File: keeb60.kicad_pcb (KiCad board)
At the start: 2 copper layers, 123 parts, among them K000 Esc, K001 1, K002 2, K003 3, K004 4, K005 5, K006 6, K007 7, K008 8, K009 9, K010 0, K011 _, K012 =, K013 Backspace, K100 Tab, K101 Q, K102 W, K103 E, K104 R, K105 T, K106 Y, K107 U, K108 I, K109 O, K110 P, K111 [, K112 ], K113 Pipe, K200 Caps Lock, K201 A, K202 S, K203 D, K204 F, K205 G, K206 H, K207 J, K208 K, K209 L, K210 ;, K211 ,, K213 Enter, K300 Shift, K302 Z, K303 X, K304 C, K305 V, K306 B, K307 N, K308 M, K309 ,, K310 ., K311 /, K313 Shift, K400 Ctrl, K401 Option, K402 Command, K406 Space, K410 Command, K411 Option, K412 Function, K413 Ctrl, U1 ProMicro

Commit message: Add edge cut
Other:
- board outline added: 290 x 99.3 mm
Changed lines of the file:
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@@
 		)
+	)
+	(gr_rect
+		(start 49.46875 84.51875)
+		(end 339.46875 183.76875)
+		(stroke
+			(width 0.05)
+			(type solid)
+		)
+		(fill no)
+		(layer "Edge.Cuts")
 	)
 	(embedded_fonts no)

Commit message: thangs
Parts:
- moved D52 73.8 mm to (242.9, 158.0)
- moved D49 38.1 mm to (281.0, 158.0)
- moved D51 35.7 mm to (316.7, 158.0)
- turned D16 to 90 degrees
- turned D43 to 90 degrees
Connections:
- D0 pad 1: (no net) -> Row0
- D0 pad 2: (no net) -> Net-(D0-A)
- D1 pad 1: (no net) -> Row0
- D1 pad 2: (no net) -> Net-(D1-A)
- D10 pad 1: (no net) -> Row0
- D10 pad 2: (no net) -> Net-(D10-A)
- D11 pad 1: (no net) -> Row0
- D11 pad 2: (no net) -> Net-(D11-A)
- D12 pad 1: (no net) -> Row0
- D12 pad 2: (no net) -> Net-(D12-A)
- D13 pad 1: (no net) -> Row1
- D13 pad 2: (no net) -> Net-(D13-A)
- D14 pad 1: (no net) -> Row1
- D14 pad 2: (no net) -> Net-(D14-A)
- D15 pad 1: (no net) -> Row1
- D15 pad 2: (no net) -> Net-(D15-A)
- D16 pad 1: (no net) -> Row1
- D16 pad 2: (no net) -> Net-(D16-A)
- D17 pad 1: (no net) -> Row1
- D17 pad 2: (no net) -> Net-(D17-A)
- D18 pad 1: (no net) -> Row1
- D18 pad 2: (no net) -> Net-(D18-A)
- D19 pad 1: (no net) -> Row1
- D19 pad 2: (no net) -> Net-(D19-A)
- D2 pad 1: (no net) -> Row0
- D2 pad 2: (no net) -> Net-(D2-A)
- D20 pad 1: (no net) -> Row1
- D20 pad 2: (no net) -> Net-(D20-A)
- D21 pad 1: (no net) -> Row1
- D21 pad 2: (no net) -> Net-(D21-A)
- D22 pad 1: (no net) -> Row1
- D22 pad 2: (no net) -> Net-(D22-A)
- D23 pad 1: (no net) -> Row1
- D23 pad 2: (no net) -> Net-(D23-A)
- D24 pad 1: (no net) -> Row1
- D24 pad 2: (no net) -> Net-(D24-A)
- D25 pad 1: (no net) -> Row1
- D25 pad 2: (no net) -> Net-(D25-A)
- D26 pad 1: (no net) -> Row2
- D26 pad 2: (no net) -> Net-(D26-A)
- D27 pad 1: (no net) -> Row2
- D27 pad 2: (no net) -> Net-(D27-A)
- D28 pad 1: (no net) -> Row2
- D28 pad 2: (no net) -> Net-(D28-A)
- D29 pad 1: (no net) -> Row2
- D29 pad 2: (no net) -> Net-(D29-A)
- D3 pad 1: (no net) -> Row0
- D3 pad 2: (no net) -> Net-(D3-A)
- D30 pad 1: (no net) -> Row2
- D30 pad 2: (no net) -> Net-(D30-A)
- D31 pad 1: (no net) -> Row2
- D31 pad 2: (no net) -> Net-(D31-A)
- D32 pad 1: (no net) -> Row2
- D32 pad 2: (no net) -> Net-(D32-A)
- D33 pad 1: (no net) -> Row2
- D33 pad 2: (no net) -> Net-(D33-A)
- D34 pad 1: (no net) -> Row2
- D34 pad 2: (no net) -> Net-(D34-A)
- D35 pad 1: (no net) -> Row2
- D35 pad 2: (no net) -> Net-(D35-A)
- D36 pad 1: (no net) -> Row2
- D36 pad 2: (no net) -> Net-(D36-A)
- D37 pad 1: (no net) -> Row2
- D37 pad 2: (no net) -> Net-(D37-A)
- D38 pad 1: (no net) -> Row2
- D38 pad 2: (no net) -> Net-(D38-A)
- D39 pad 1: (no net) -> Row3
- D39 pad 2: (no net) -> Net-(D39-A)
- D4 pad 1: (no net) -> Row0
- D4 pad 2: (no net) -> Net-(D4-A)
- D40 pad 1: (no net) -> Row3
- D40 pad 2: (no net) -> Net-(D40-A)
- D41 pad 1: (no net) -> Row3
- D41 pad 2: (no net) -> Net-(D41-A)
- D42 pad 1: (no net) -> Row3
- D42 pad 2: (no net) -> Net-(D42-A)
- D43 pad 1: (no net) -> Row3
- D43 pad 2: (no net) -> Net-(D43-A)
- D44 pad 1: (no net) -> Row3
- D44 pad 2: (no net) -> Net-(D44-A)
- D45 pad 1: (no net) -> Row3
- D45 pad 2: (no net) -> Net-(D45-A)
- D46 pad 1: (no net) -> Row3
- D46 pad 2: (no net) -> Net-(D46-A)
- D47 pad 1: (no net) -> Row3
- D47 pad 2: (no net) -> Net-(D47-A)
- D48 pad 1: (no net) -> Row3
- D48 pad 2: (no net) -> Net-(D48-A)
- D49 pad 1: (no net) -> Row3
- D49 pad 2: (no net) -> Net-(D49-A)
- D5 pad 1: (no net) -> Row0
- D5 pad 2: (no net) -> Net-(D5-A)
- D50 pad 1: (no net) -> Row3
- D50 pad 2: (no net) -> Net-(D50-A)
- D53 pad 1: (no net) -> Row4
- D53 pad 2: (no net) -> Net-(D53-A)
- D54 pad 1: (no net) -> Row4
- D54 pad 2: (no net) -> Net-(D54-A)
- D55 pad 1: (no net) -> Row4
- D55 pad 2: (no net) -> Net-(D55-A)
- D56 pad 1: (no net) -> Row4
- D56 pad 2: (no net) -> Net-(D56-A)
- D57 pad 1: (no net) -> Row4
- D57 pad 2: (no net) -> Net-(D57-A)
- D58 pad 1: (no net) -> Row4
- D58 pad 2: (no net) -> Net-(D58-A)
- D59 pad 1: (no net) -> Row4
- D59 pad 2: (no net) -> Net-(D59-A)
- D6 pad 1: (no net) -> Row0
- D6 pad 2: (no net) -> Net-(D6-A)
- D60 pad 1: (no net) -> Row4
- D60 pad 2: (no net) -> Net-(D60-A)
- D7 pad 1: (no net) -> Row0
- D7 pad 2: (no net) -> Net-(D7-A)
- D8 pad 1: (no net) -> Row0
- D8 pad 2: (no net) -> Net-(D8-A)
- D9 pad 1: (no net) -> Row0
- D9 pad 2: (no net) -> Net-(D9-A)
- K101 pad 1: (no net) -> Net-(D14-A)
- K101 pad 2: (no net) -> Col1
- K204 pad 1: (no net) -> Net-(D30-A)
- K204 pad 2: (no net) -> Col4
- K209 pad 1: (no net) -> Net-(D35-A)
- K209 pad 2: (no net) -> Col9
- U1 pad 24: Net-(U1-5V) -> unconnected-(U1-5V-Pad24)
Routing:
- net Row0: track 0.00 -> 228.6 mm
- net Row1: track 0.00 -> 214.3 mm
- net Row3: track 0.00 -> 203.1 mm
- net Row2: track 0.00 -> 197.6 mm
- net Col0: track 0.00 -> 89.2 mm
- net Col10: track 0.00 -> 48.2 mm
- net Col9: track 0.00 -> 48.1 mm
- net Col4: track 0.00 -> 48.1 mm
- net Col3: track 0.00 -> 48.1 mm
- net Col6: track 0.00 -> 48.1 mm
- net Col2: track 0.00 -> 48.1 mm
- net Col11: track 0.00 -> 48.1 mm
- net Col5: track 0.00 -> 48.1 mm
- net Col8: track 0.00 -> 48.1 mm
- net Col7: track 0.00 -> 48.1 mm
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
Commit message: Fix diodes
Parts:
- moved D13 253.1 mm to (71.4, 119.9)
- moved D51 247.6 mm to (69.8, 177.0)
- moved D26 231.8 mm to (73.8, 138.9)
- moved D27 229.4 mm to (100.0, 138.9)
- moved D40 212.8 mm to (109.5, 158.0)
- moved D39 212.8 mm to (78.6, 158.0)
- moved D52 151.2 mm to (92.9, 177.0)
- moved D55 142.9 mm to (259.6, 177.0)
- moved D54 95.2 mm to (188.1, 177.0)
- moved D56 95.2 mm to (283.4, 177.0)
- moved D60 76.5 mm to (323.9, 100.9)
- moved D59 61.0 mm to (328.6, 119.9)
- moved D50 54.8 mm to (316.7, 158.0)
- moved D41 50.8 mm to (129.4, 158.0)
- moved D38 50.0 mm to (321.5, 138.9)
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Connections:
- D13 pad 1: Row1 -> (no net)
- D13 pad 2: Net-(D13-A) -> (no net)
- D26 pad 1: Row2 -> (no net)
- D26 pad 2: Net-(D26-A) -> (no net)
- D28 pad 1: Row2 -> (no net)
- D28 pad 2: Net-(D28-A) -> (no net)
- D30 pad 1: Row2 -> (no net)
- D30 pad 2: Net-(D30-A) -> (no net)
- D39 pad 1: Row3 -> (no net)
- D39 pad 2: Net-(D39-A) -> (no net)
- D40 pad 1: Row3 -> (no net)
- D40 pad 2: Net-(D40-A) -> (no net)
- D41 pad 1: Row3 -> (no net)
- D41 pad 2: Net-(D41-A) -> (no net)
- D42 pad 1: Row3 -> (no net)
- D42 pad 2: Net-(D42-A) -> (no net)
- D50 pad 1: Row3 -> (no net)
- D50 pad 2: Net-(D50-A) -> (no net)
- D59 pad 1: Row4 -> (no net)
- D59 pad 2: Net-(D59-A) -> (no net)
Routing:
- net Row1: track 214.3 -> 233.4 mm

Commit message: More routing
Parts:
- moved U1 2.80 mm to (210.8, 173.5), turned to -90 degrees
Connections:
- D13 pad 1: (no net) -> Row1
- D13 pad 2: (no net) -> Net-(D13-A)
- D26 pad 1: (no net) -> Row2
- D26 pad 2: (no net) -> Net-(D26-A)
- D28 pad 1: (no net) -> Row2
- D28 pad 2: (no net) -> Net-(D28-A)
- D30 pad 1: (no net) -> Row2
- D30 pad 2: (no net) -> Net-(D30-A)
- D39 pad 1: (no net) -> Row3
- D39 pad 2: (no net) -> Net-(D39-A)
- D40 pad 1: (no net) -> Row3
- D40 pad 2: (no net) -> Net-(D40-A)
- D41 pad 1: (no net) -> Row3
- D41 pad 2: (no net) -> Net-(D41-A)
- D42 pad 1: (no net) -> Row3
- D42 pad 2: (no net) -> Net-(D42-A)
- D50 pad 1: (no net) -> Row3
- D50 pad 2: (no net) -> Net-(D50-A)
- D51 pad 1: (no net) -> Row4
- D51 pad 2: (no net) -> Net-(D51-A)
- D52 pad 1: (no net) -> Row4
- D52 pad 2: (no net) -> Net-(D52-A)
- D59 pad 1: (no net) -> Row4
- D59 pad 2: (no net) -> Net-(D59-A)
- K302 pad 2: Col2 -> Col1
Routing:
- net Row4: track 0.00 -> 71.4 mm
- net Col1: track 48.1 -> 100.4 mm
- net Col6: track 48.1 -> 92.9 mm
- net Col9: track 48.1 -> 71.1 mm
- net Col8: track 48.1 -> 71.1 mm
- net Col7: track 48.1 -> 71.1 mm
- net Col4: track 48.1 -> 71.1 mm
- net Col11: track 48.1 -> 71.1 mm
- net Col3: track 48.1 -> 71.1 mm
- net Col5: track 48.1 -> 71.1 mm
- net Col10: track 48.2 -> 71.2 mm
- net Row2: track 197.6 -> 216.7 mm
- net Row3: track 203.1 -> 203.8 mm

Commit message: ROUTING!
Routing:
- net Row4: track 71.4 -> 191.1 mm
- net Row3: track 203.8 -> 240.9 mm
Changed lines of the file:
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@@
+	)
+	(segment
+		(start 288.8625 159.60625)
+		(end 280.9875 159.60625)
+		(width 0.254)
+		(layer "B.Cu")
+		(net 45)
+	)
+	(segment
+		(start 315.05625 157.95625)
+		(end 290.5125 157.95625)
+		(width 0.254)
+		(layer "B.Cu")
+		(net 45)
+	)
+	(segment
+		(start 290.5125 157.95625)
+		(end 288.8625 159.60625)
+		(width 0.254)
+		(layer "B.Cu")
+		(net 45)
 	)
 	(segment
@@
 	)
 	(segment
+		(start 316.70625 159.60625)
+		(end 315.05625 157.95625)
+		(width 0.254)
+		(layer "B.Cu")
+		(net 45)
+	)
+	(segment
 		(start 59.53125 140.462)
 		(end 67.183 148.11375)
@@
 	)
 	(segment
+		(start 122.175 178.65625)
+		(end 116.68125 178.65625)
+		(width 0.254)
+		(layer "B.Cu")
+		(net 82)
+	)
+	(segment
+		(start 180.975 177.00625)
+		(end 123.825 177.00625)
+		(width 0.254)
+		(layer "B.Cu")
+		(net 82)
+	)
+	(segment
+		(start 69.85 178.65625)
+		(end 116.68125 178.65625)
+		(width 0.254)
+		(layer "B.Cu")
+		(net 82)
+	)
+	(segment
+		(start 188.11875 178.65625)
+		(end 182.625 178.65625)
+		(width 0.254)
+		(layer "B.Cu")
+		(net 82)
+	)
+	(segment
 		(start 330.99375 178.65625)
 		(end 259.55625 178.65625)
 		(width 0.254)
 		(layer "B.Cu")
+		(net 82)
+	)
+	(segment
+		(start 182.625 178.65625)
+		(end 180.975 177.00625)
+		(width 0.254)
+		(layer "B.Cu")
+		(net 82)
+	)
+	(segment
+		(start 123.825 177.00625)
+		(end 122.175 178.65625)
+		(width 0.254)
+		(layer "B.Cu")

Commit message: ROUTES BBY
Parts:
- moved U1 2.97 mm to (210.0, 170.7), turned to 90 degrees
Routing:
- net Row4: track 191.1 -> 279.3 mm
- net Col12: track 24.7 -> 79.3 mm
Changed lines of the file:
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@@
 	(footprint "TheOneProMicro-main:TheOneProMicro"
 		(layer "F.Cu")
-		(at 210.82 173.51375 -90)
+		(at 210.02625 170.65625 90)
 		(descr "Pro Micro footprint")
 		(tags "promicro ProMicro")
@@
 		)
 		(property "Datasheet" ""
-			(at -1.27 1.27 180)
+			(at -1.27 1.27 0)
 			(unlocked yes)
 			(layer "F.Fab")
@@
 		)
 		(property "Description" ""
-			(at -1.27 1.27 180)
+			(at -1.27 1.27 0)
 			(unlocked yes)
 			(layer "F.Fab")
@@
 		)
 		(pad "1" thru_hole circle
-			(at 6.35 -12.7 180)
+			(at 6.35 -12.7)
 			(size 1.6 1.6)
 			(drill 1.1)
@@
 		)
 		(pad "2" thru_hole circle
-			(at 6.35 -10.16 180)
+			(at 6.35 -10.16)
 			(size 1.6 1.6)
 			(drill 1.1)
@@
 		)
 		(pad "3" thru_hole circle
-			(at 6.35 -7.62 180)
+			(at 6.35 -7.62)
 			(size 1.6 1.6)
 			(drill 1.1)
@@
 		)
 		(pad "4" thru_hole circle
-			(at 6.35 -5.08 180)
+			(at 6.35 -5.08)
 			(size 1.6 1.6)
 			(drill 1.1)
@@
 		)
 		(pad "5" thru_hole circle
-			(at 6.35 -2.54 180)
+			(at 6.35 -2.54)
 			(size 1.6 1.6)
 			(drill 1.1)
@@
 		)
 		(pad "6" thru_hole circle
-			(at 6.35 0 180)
+			(at 6.35 0)
 			(size 1.6 1.6)
 			(drill 1.1)
@@
 		)
 		(pad "7" thru_hole circle
-			(at 6.35 2.54 180)
+			(at 6.35 2.54)
 			(size 1.6 1.6)
 			(drill 1.1)
@@
 		)
 		(pad "8" thru_hole circle
-			(at 6.35 5.08 180)
+			(at 6.35 5.08)
 			(size 1.6 1.6)
 			(drill 1.1)
@@
 		)
 		(pad "9" thru_hole circle
-			(at 6.35 7.62 180)
+			(at 6.35 7.62)
 			(size 1.6 1.6)
 			(drill 1.1)
@@
 		)
 		(pad "10" thru_hole circle
-			(at 6.35 10.16 180)
+			(at 6.35 10.16)
 			(size 1.6 1.6)
 			(drill 1.1)
@@
 		)
 		(pad "11" thru_hole circle
-			(at 6.35 12.7 180)
+			(at 6.35 12.7)
 			(size 1.6 1.6)
 			(drill 1.1)
@@
 		)
 		(pad "12" thru_hole circle
-			(at 6.35 15.24 180)
+			(at 6.35 15.24)
 			(size 1.6 1.6)
 			(drill 1.1)
@@
 		)
 		(pad "13" thru_hole circle
-			(at -8.89 15.24 180)
+			(at -8.89 15.24)
 			(size 1.6 1.6)
 			(drill 1.1)
@@
 		)
 		(pad "14" thru_hole circle
-			(at -8.89 12.7 180)
+			(at -8.89 12.7)
 			(size 1.6 1.6)
 			(drill 1.1)
@@
 		)
 		(pad "15" thru_hole circle
-			(at -8.89 10.16 180)
+			(at -8.89 10.16)
 			(size 1.6 1.6)
 			(drill 1.1)
@@
 		)
 		(pad "16" thru_hole circle
-			(at -8.89 7.62 180)
+			(at -8.89 7.62)
 			(size 1.6 1.6)
 			(drill 1.1)
@@
 		)
 		(pad "17" thru_hole circle
-			(at -8.89 5.08 180)
+			(at -8.89 5.08)
 			(size 1.6 1.6)
 			(drill 1.1)
@@
 		)
 		(pad "18" thru_hole circle
-			(at -8.89 2.54 180)
+			(at -8.89 2.54)
 			(size 1.6 1.6)
 			(drill 1.1)
@@
 		)
 		(pad "19" thru_hole circle
-			(at -8.89 0 180)
+			(at -8.89 0)
 			(size 1.6 1.6)
 			(drill 1.1)
@@
 		)
 		(pad "20" thru_hole circle
-			(at -8.89 -2.54 180)
+			(at -8.89 -2.54)
 			(size 1.6 1.6)
 			(drill 1.1)
@@
 		)
 		(pad "21" thru_hole circle
-			(at -8.89 -5.08 180)
+			(at -8.89 -5.08)
 			(size 1.6 1.6)
 			(drill 1.1)
@@
 		)
 		(pad "22" thru_hole circle
-			(at -8.89 -7.62 180)
+			(at -8.89 -7.62)
 			(size 1.6 1.6)
 			(drill 1.1)
@@
 		)
 		(pad "23" thru_hole circle
-			(at -8.89 -10.16 180)
+			(at -8.89 -10.16)
 			(size 1.6 1.6)
 			(drill 1.1)
@@
 		)
 		(pad "24" thru_hole rect
-			(at -8.89 -12.7 180)
+			(at -8.89 -12.7)
 			(size 1.6 1.6)
 			(drill 1.1)
@@
 	)
 	(segment
+		(start 302.41875 130.96875)
+		(end 308.1655 130.96875)
+		(width 0.254)
+		(layer "F.Cu")
+		(net 78)
+	)
+	(segment
+		(start 310.0705 129.06375)
+		(end 307.975 131.15925)
+		(width 0.254)
+		(layer "F.Cu")
+		(net 78)
+	)
+	(segment
+		(start 292.93085 121.48085)
+		(end 302.41875 130.96875)
+		(width 0.254)
+		(layer "F.Cu")
+		(net 78)
+	)
+	(segment
+		(start 308.1655 130.96875)
+		(end 310.0705 129.06375)
+		(width 0.254)
+		(layer "F.Cu")
+		(net 78)
+	)
+	(segment
+		(start 293.40175 110.01375)
+		(end 292.93085 110.48465)
+		(width 0.254)
+		(layer "F.Cu")
+		(net 78)
+	)
+	(segment
+		(start 292.93085 110.48465)
+		(end 292.93085 121.48085)
+		(width 0.254)
+		(layer "F.Cu")
+		(net 78)
+	)
+	(segment
 		(start 281.78125 98.39325)
 		(end 293.40175 110.01375)
@@
 	)
 	(segment
+		(start 307.975 145.44675)
+		(end 305.308 148.11375)
+		(width 0.254)
+		(layer "F.Cu")
+		(net 78)
+	)
+	(segment
 		(start 281.78125 93.05925)
 		(end 281.78125 98.39325)
@@
 	)
 	(segment
+		(start 307.975 131.15925)
+		(end 307.975 145.44675)
+		(width 0.254)
+		(layer "F.Cu")
+		(net 78)
+	)
+	(segment
+		(start 333.375 116.74375)
+		(end 328.6125 121.50625)
+		(width 0.2)
+		(layer "B.Cu")
+		(net 82)
+	)
+	(segment
 		(start 122.175 178.65625)
 		(end 116.68125 178.65625)
@@
 	)
 	(segment
+		(start 323.85 102.51875)
+		(end 330.075 108.74375)
+		(width 0.2)
+		(layer "B.Cu")
+		(net 82)
+	)
+	(segment
 		(start 69.85 178.65625)
 		(end 116.68125 178.65625)
@@
 	)
 	(segment
+		(start 334.9625 173.83125)
+		(end 330.99375 177.8)
+		(width 0.2)
+		(layer "B.Cu")
+		(net 82)
+	)
+	(segment
 		(start 188.11875 178.65625)
 		(end 182.625 178.65625)
@@
 	)
 	(segment
+		(start 330.99375 177.8)
+		(end 330.99375 178.65625)
+		(width 0.2)
+		(layer "B.Cu")
+		(net 82)
+	)
+	(segment
 		(start 182.625 178.65625)
 		(end 180.975 177.00625)
@@
 		(layer "B.Cu")
 		(net 82)
+	)
+	(segment
+		(start 330.075 108.74375)
+		(end 333.375 108.74375)
+		(width 0.2)
+		(layer "B.Cu")
+		(net 82)
+	)
+	(segment
+		(start 334.9625 127.85625)
+		(end 334.9625 173.83125)
+		(width 0.2)
+		(layer "B.Cu")
+		(net 82)
+	)
+	(segment
+		(start 328.6125 121.50625)
+		(end 334.9625 127.85625)
+		(width 0.2)
+		(layer "B.Cu")
+		(net 82)
+	)
+	(segment
+		(start 333.375 108.74375)
+		(end 333.375 116.74375)
+		(width 0.2)
+		(layer "B.Cu")
+		(net 82)

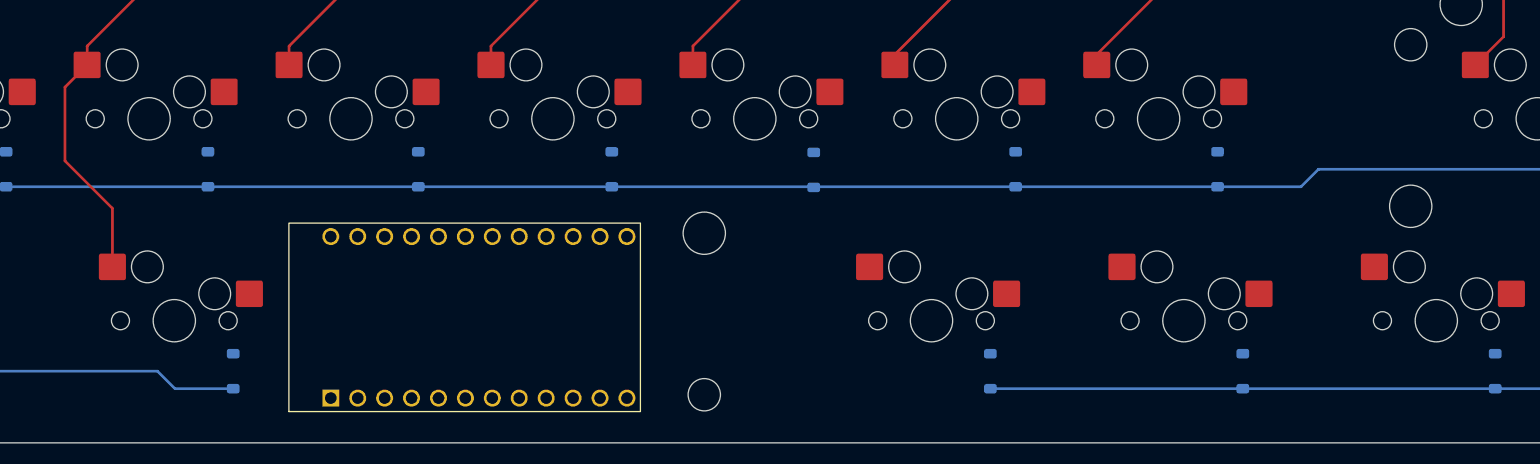
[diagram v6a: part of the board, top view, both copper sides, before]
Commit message: Start routing cols
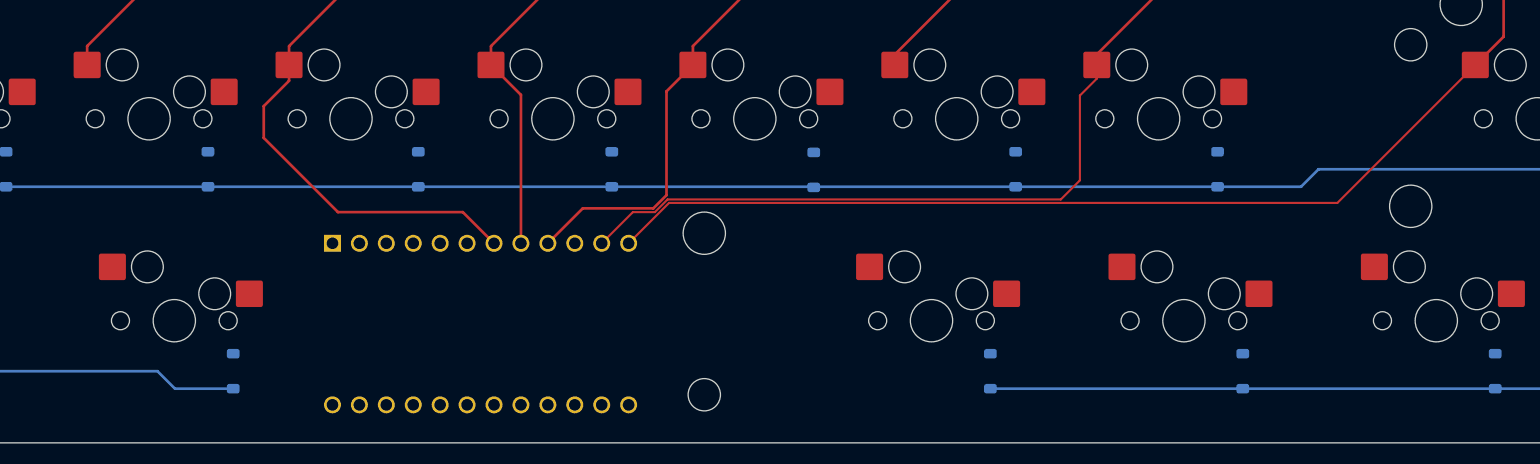
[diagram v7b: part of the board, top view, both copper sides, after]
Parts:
- U1: moved to B.Cu
- moved U1 3.18 mm to (210.2, 173.8), turned to -90 degrees
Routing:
- net Col12: track 79.3 -> 166.1 mm
- net Col11: track 71.1 -> 130.3 mm
- net Col7: track 71.1 -> 104.9 mm
- net Col9: track 71.1 -> 97.5 mm
- net Col6: track 92.9 -> 71.1 mm
- net Col8: track 71.1 -> 89.1 mm

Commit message: ~~magic~~
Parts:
- moved U1 2.14 mm to (212.3, 173.5)
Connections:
- K406 pad 2: Col6 -> Col5
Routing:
- net Row4: track 279.3 -> 354.5 mm
- net Col5: track 71.1 -> 144.0 mm
- net Col6: track 71.1 -> 123.3 mm
- net Col10: track 71.2 -> 110.2 mm
- net Col12: track 166.1 -> 192.6 mm
- net Col9: track 97.5 -> 95.0 mm
- net Col7: track 104.9 -> 106.8 mm
- net Col11: track 130.3 -> 129.1 mm
- net Col8: track 89.1 -> 89.7 mm
